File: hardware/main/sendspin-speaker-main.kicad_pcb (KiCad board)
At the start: 2 copper layers, 100 x 58 mm, 88 parts, among them J201 J_BAT, J202 J_SW, J203 J_CHG, J301 J_USB, J401 J_SPK_L, J402 J_SPK_R, J403 PJ-320D, J501 J_UI, J502 J_LED, Q201 FS8205A, Q202 AO3401A, Q301 UMH3N, SW101 Reset, SW102 Boot, SW201 MSK12C02, U101 ESP32-A1S, U201 TP4056, U202 DW01A, U203 AP2112K-3.3, U301 USBLC6-2SC6, U302 CH340C, U303 XC6206P332MR, U401 NS4150B, U402 NS4150B

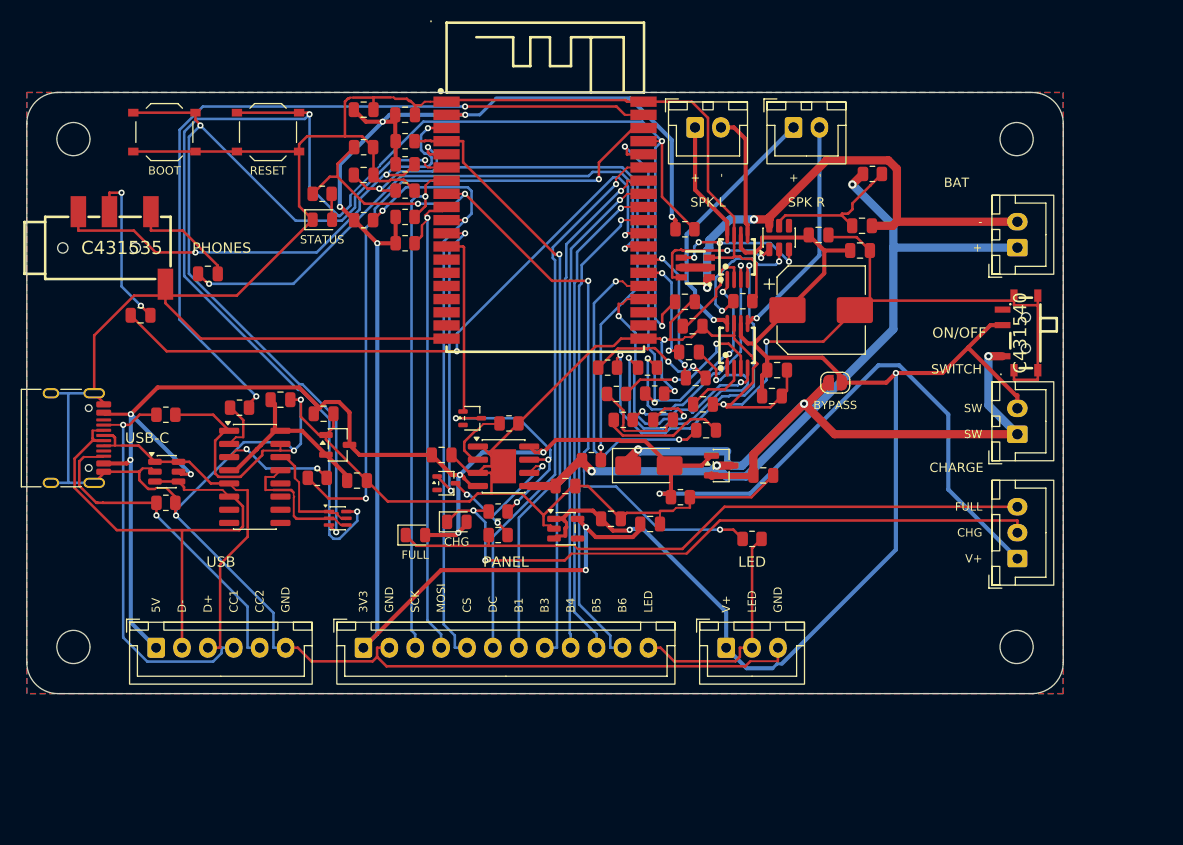
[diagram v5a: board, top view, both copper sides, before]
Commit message: hardware: headphone jack removed, main board 70 x 60 mm
- J403, C422, C423 out; HPOUTL/R open, GPIO39 spare with its pull-up.
- Main board re-placed on 70 x 60 mm (decoupling placed first), routed,
  labelled; route.py cleans dangling vias and sub-minimum tracks.
- LCSC fields rewritten after regenerating MCU and Audio sheets.

Co-Authored-By: Claude Opus 5.5 <noreply@anthropic.com>
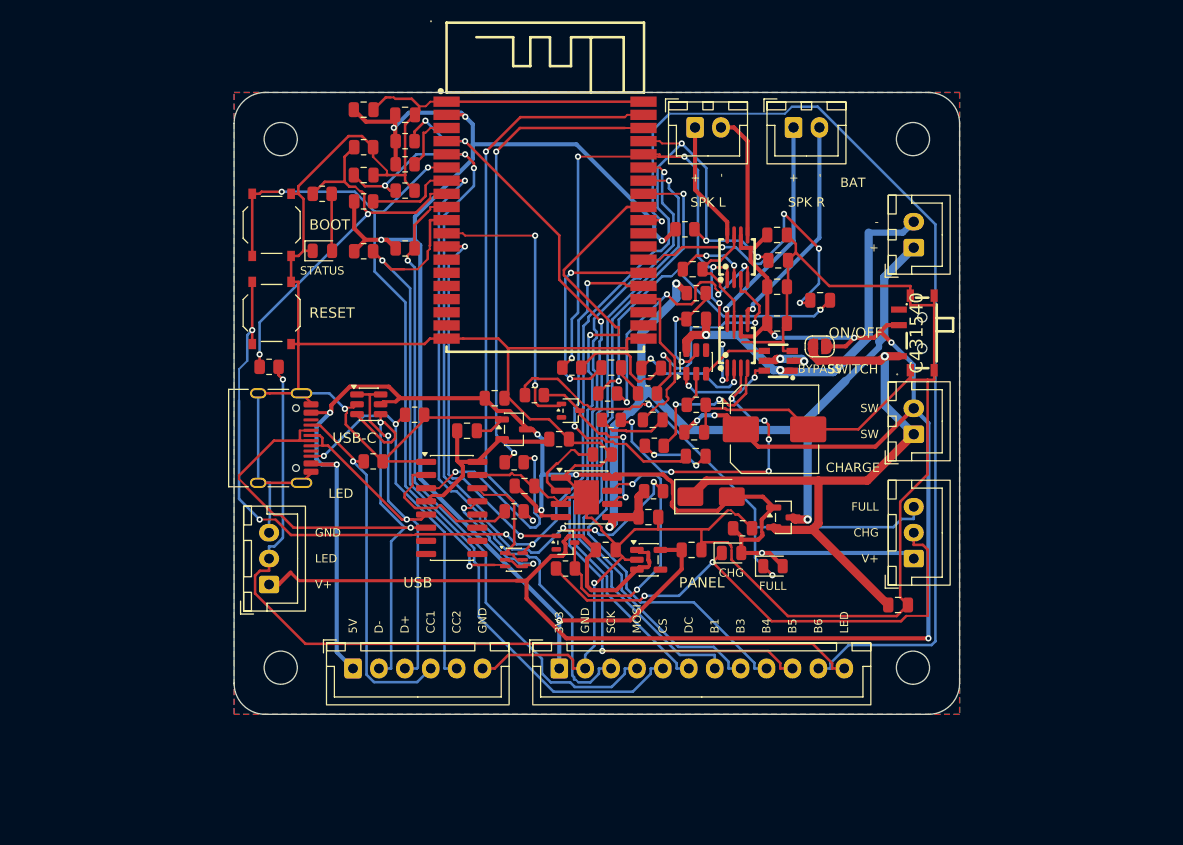
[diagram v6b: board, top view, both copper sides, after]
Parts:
- removed C422, C423: 47u, Capacitor_SMD:C_0805_2012Metric
- removed J403: PJ-320D, lcsc:AUDIO-SMD_PJ-320D-1
- moved R501 49.5 mm to (123.4, 126.5)
- moved J502 44.5 mm to (123.4, 147.5), turned to 90 degrees
- moved D202 34.6 mm to (172.0, 145.7)
- moved R303 28.3 mm to (147.0, 140.4)
- moved D201 26.7 mm to (168.0, 144.4)
- moved R302 25.5 mm to (137.4, 131.1)
- moved U301 20.6 mm to (133.0, 130.1)
- moved R204 20.5 mm to (164.6, 119.4)
- moved R301 20.5 mm to (133.4, 135.6)
- moved H3 20.1 mm to (124.5, 155.5)
- moved H1 20.0 mm to (124.5, 104.5)
- moved USB301 20.0 mm to (123.4, 133.3)
- moved C302 19.9 mm to (151.4, 133.4)
- moved U302 19.2 mm to (141.0, 140.1)
- moved J301 19.1 mm to (131.5, 155.6)
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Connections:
- net /HP_DET renamed /MCU/GPIO39
- U101 pad 27: /HPOUTL -> unconnected-(U101-HPOUTL-Pad27)
- U101 pad 28: /HPOUTR -> unconnected-(U101-HPOUTR-Pad28)
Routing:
- net GND: track 503.4 -> 401.8 mm, vias 7 -> 2
- net /HPOUTR: track 64.4 -> 0.00 mm, vias 2 -> 0
- net /Connectors/LED_EXT: track 22.5 -> 84.1 mm, vias 0 -> 1
- net /HPOUTL: track 55.7 -> 0.00 mm, vias 2 -> 0
- net /VBUS: track 175.2 -> 125.3 mm, vias 7 -> 6
- net /BTN6: track 47.5 -> 96.8 mm
- net VBAT_SW: track 135.0 -> 181.9 mm, vias 2 -> 6
- net /MCU/GPIO39: track 50.2 -> 5.82 mm, vias 3 -> 0
- net /LED: track 74.9 -> 39.4 mm, vias 4 -> 2
- net /EN: track 150.3 -> 122.7 mm, vias 4 -> 7
- net /BTN5: track 47.4 -> 73.8 mm, vias 1 -> 2
- net /Audio/LP_C: track 27.9 -> 3.18 mm, vias 2 -> 0
- net /Audio/LN_C: track 12.8 -> 33.8 mm
- net /U0RXD: track 76.2 -> 55.4 mm
- net /DISP_SCK: track 50.5 -> 71.0 mm
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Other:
- board size 100 x 58 mm -> 70 x 60 mm
- board text removed: "PHONES"
